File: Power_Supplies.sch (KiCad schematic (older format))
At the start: 82 parts, among them J1 Conn_HDR_2x10_latching, M1 2N7002BK, M2 2N7002BK, Q11 2N7002BK, Q12 2N7002BK, Q13 2N7002BK, Q14 2N7002BK, Q6 2N7002BK, Q7 2N7002BK, Q8 2N7002BK, Q9 2N7002BK, U22 BD50FC0WEFJ-E2, U23 LDL212D33R

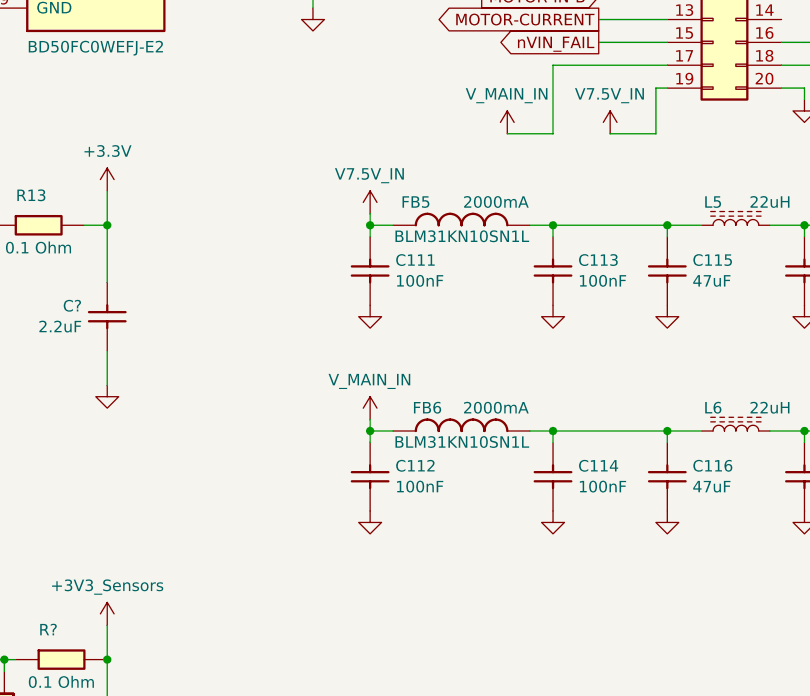
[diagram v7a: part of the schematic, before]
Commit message: Updated BLM31KN102SN1L library part and replaced pre-existing one on Power Supplies sheet
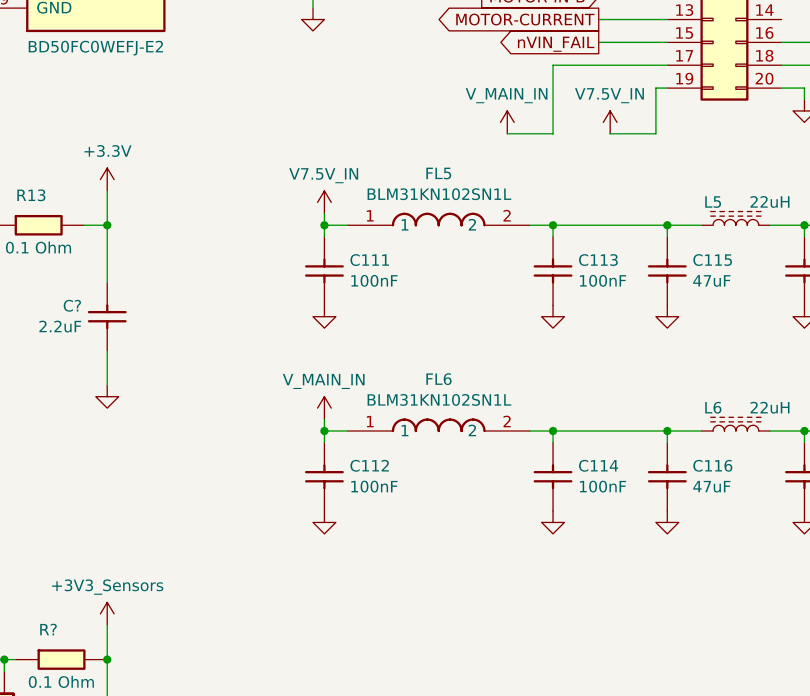
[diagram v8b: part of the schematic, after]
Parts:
- removed FB5, FB6: BLM31KN10SN1L, symbol OpenVent:BLM31KN10SN1L
- added FL5, FL6: BLM31KN102SN1L, BLM31KN102BH1L, symbol OpenVent:BLM31KN102SN1L
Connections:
- net +5V: now also FL5.1
- net V_MAIN: now also FL6.1
- net at C113.1, C115.1, L5.1: now also FL5.2
- net at C114.1, C116.1, L6.1: now also FL6.2
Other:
- moved on the sheet: C111, C112
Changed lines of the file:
@@
 L OpenVent:100nF_0603_Ceramic_Capacitor,_10%,_X7R,_25V C111
 U 1 1 606AB5CB
-P 8350 2550
-F 0 "C111" V 8354 2560 50  0000 L CNN
-F 1 "100nF_0603_Ceramic_Capacitor,_10%,_X7R,_25V" H 8350 2550 50  0001 C CNN
-F 2 "" H 8350 2550 50  0001 C CNN
-F 3 "" H 8350 2550 50  0001 C CNN
-F 4 "100nF" V 8445 2560 50  0000 L CNN "Val"
-F 5 "25V" H 8350 2550 50  0001 C CNN "Voltage"
-F 6 "10%" H 8350 2550 50  0001 C CNN "Tolerance"
-	1    8350 2550
+P 8150 2550
+F 0 "C111" V 8154 2560 50  0000 L CNN
+F 1 "100nF_0603_Ceramic_Capacitor,_10%,_X7R,_25V" H 8150 2550 50  0001 C CNN
+F 2 "" H 8150 2550 50  0001 C CNN
+F 3 "" H 8150 2550 50  0001 C CNN
+F 4 "100nF" V 8245 2560 50  0000 L CNN "Val"
+F 5 "25V" H 8150 2550 50  0001 C CNN "Voltage"
+F 6 "10%" H 8150 2550 50  0001 C CNN "Tolerance"
+	1    8150 2550
 	0    1    1    0
 $EndComp
@@
 	0    -1   -1   0
 $EndComp
-$Comp
-L OpenVent:BLM31KN10SN1L FB5
-U 1 1 60812B24
-P 8600 2400
-F 0 "FB5" H 8450 2500 50  0000 C CNN
-F 1 "BLM31KN10SN1L" H 8650 2350 50  0000 C CNN
-F 2 "" H 8350 2400 50  0001 C CNN
-F 3 "https://drive.google.com/drive/u/1/folders/1bT0MezjjDfDXdTdQktjf6O5y5oTJs8ND" H 8350 2400 50  0001 C CNN
-F 4 "75mR" H 8825 2525 50  0001 L CNN "Val"
-F 5 "2000mA" H 8800 2500 50  0000 C CNN "Current"
-	1    8600 2400
-	1    0    0    -1
-$EndComp
-Wire Wire Line
-	8350 2400 8250 2400
-Wire Wire Line
-	8250 2400 8250 2350
-Wire Wire Line
-	8250 2450 8250 2400
-Connection ~ 8250 2400
+Wire Wire Line
+	8150 2400 8050 2400
+Wire Wire Line
+	8050 2400 8050 2350
+Wire Wire Line
+	8050 2450 8050 2400
+Connection ~ 8050 2400
 Wire Wire Line
 	8950 2400 9050 2400
@@
 L OpenVent:GND #PWR0198
 U 1 1 6087AC95
-P 8250 2750
-F 0 "#PWR0198" H 8250 2500 50  0001 C CNN
-F 1 "GND" H 8250 2600 50  0001 C CNN
-F 2 "" H 8250 2750 50  0001 C CNN
-F 3 "" H 8250 2750 50  0001 C CNN
-	1    8250 2750
+P 8050 2750
+F 0 "#PWR0198" H 8050 2500 50  0001 C CNN
+F 1 "GND" H 8050 2600 50  0001 C CNN
+F 2 "" H 8050 2750 50  0001 C CNN
+F 3 "" H 8050 2750 50  0001 C CNN
+	1    8050 2750
 	1    0    0    -1
 $EndComp
@@
 L OpenVent:V7.5V_IN #PWR0197
 U 1 1 608A108E
-P 8250 2350
-F 0 "#PWR0197" H 8250 2200 50  0001 C CNN
-F 1 "V7.5V_IN" H 8250 2523 50  0000 C CNN
-F 2 "" H 8250 2350 50  0001 C CNN
-F 3 "" H 8250 2350 50  0001 C CNN
-	1    8250 2350
+P 8050 2350
+F 0 "#PWR0197" H 8050 2200 50  0001 C CNN
+F 1 "V7.5V_IN" H 8050 2523 50  0000 C CNN
+F 2 "" H 8050 2350 50  0001 C CNN
+F 3 "" H 8050 2350 50  0001 C CNN
+	1    8050 2350
 	1    0    0    -1
 $EndComp
@@
 L OpenVent:100nF_0603_Ceramic_Capacitor,_10%,_X7R,_25V C112
 U 1 1 6090A7D3
-P 8350 3450
-F 0 "C112" V 8354 3460 50  0000 L CNN
-F 1 "100nF_0603_Ceramic_Capacitor,_10%,_X7R,_25V" H 8350 3450 50  0001 C CNN
-F 2 "" H 8350 3450 50  0001 C CNN
-F 3 "" H 8350 3450 50  0001 C CNN
-F 4 "100nF" V 8445 3460 50  0000 L CNN "Val"
-F 5 "25V" H 8350 3450 50  0001 C CNN "Voltage"
-F 6 "10%" H 8350 3450 50  0001 C CNN "Tolerance"
-	1    8350 3450
+P 8150 3450
+F 0 "C112" V 8154 3460 50  0000 L CNN
+F 1 "100nF_0603_Ceramic_Capacitor,_10%,_X7R,_25V" H 8150 3450 50  0001 C CNN
+F 2 "" H 8150 3450 50  0001 C CNN
+F 3 "" H 8150 3450 50  0001 C CNN
+F 4 "100nF" V 8245 3460 50  0000 L CNN "Val"
+F 5 "25V" H 8150 3450 50  0001 C CNN "Voltage"
+F 6 "10%" H 8150 3450 50  0001 C CNN "Tolerance"
+	1    8150 3450
 	0    1    1    0
 $EndComp
@@
 	0    1    1    0
 $EndComp
-$Comp
-L OpenVent:BLM31KN10SN1L FB6
-U 1 1 6090A817
-P 8600 3300
-F 0 "FB6" H 8500 3400 50  0000 C CNN
-F 1 "BLM31KN10SN1L" H 8650 3250 50  0000 C CNN
-F 2 "" H 8350 3300 50  0001 C CNN
-F 3 "https://drive.google.com/drive/u/1/folders/1bT0MezjjDfDXdTdQktjf6O5y5oTJs8ND" H 8350 3300 50  0001 C CNN
-F 4 "75mR" H 8825 3425 50  0001 L CNN "Val"
-F 5 "2000mA" H 8800 3400 50  0000 C CNN "Current"
-	1    8600 3300
-	1    0    0    -1
-$EndComp
-Wire Wire Line
-	8350 3300 8250 3300
-Wire Wire Line
-	8250 3300 8250 3250
-Wire Wire Line
-	8250 3350 8250 3300
-Connection ~ 8250 3300
+Wire Wire Line
+	8150 3300 8050 3300
+Wire Wire Line
+	8050 3300 8050 3250
+Wire Wire Line
+	8050 3350 8050 3300
+Connection ~ 8050 3300
 Wire Wire Line
 	8950 3300 9050 3300
@@
 L OpenVent:GND #PWR0200
 U 1 1 6090A846
-P 8250 3650
-F 0 "#PWR0200" H 8250 3400 50  0001 C CNN
-F 1 "GND" H 8250 3500 50  0001 C CNN
-F 2 "" H 8250 3650 50  0001 C CNN
-F 3 "" H 8250 3650 50  0001 C CNN
-	1    8250 3650
+P 8050 3650
+F 0 "#PWR0200" H 8050 3400 50  0001 C CNN
+F 1 "GND" H 8050 3500 50  0001 C CNN
+F 2 "" H 8050 3650 50  0001 C CNN
+F 3 "" H 8050 3650 50  0001 C CNN
+	1    8050 3650
 	1    0    0    -1
 $EndComp
@@
 L OpenVent:V_MAIN_IN #PWR0199
 U 1 1 6094290D
-P 8250 3250
-F 0 "#PWR0199" H 8250 3100 50  0001 C CNN
-F 1 "V_MAIN_IN" H 8250 3423 50  0000 C CNN
-F 2 "" H 8250 3250 50  0001 C CNN
-F 3 "" H 8250 3250 50  0001 C CNN
-	1    8250 3250
+P 8050 3250
+F 0 "#PWR0199" H 8050 3100 50  0001 C CNN
+F 1 "V_MAIN_IN" H 8050 3423 50  0000 C CNN
+F 2 "" H 8050 3250 50  0001 C CNN
+F 3 "" H 8050 3250 50  0001 C CNN
+	1    8050 3250
 	1    0    0    -1
 $EndComp
@@
 Wire Wire Line
 	3950 2650 3950 2850
+$Comp
+L OpenVent:BLM31KN102SN1L FL5
+U 1 1 60A84874
+P 8550 2400
+F 0 "FL5" H 8550 2625 50  0000 C CNN
+F 1 "BLM31KN102SN1L" H 8550 2534 50  0000 C CNN
+F 2 "BLM31KN102BH1L" H 9200 2500 50  0001 L CNN
+F 3 "https://www.murata.com/en-us/products/productdetail?partno=BLM31KN102SN1%23" H 9200 2400 50  0001 L CNN
+F 4 "BLM31_N1L Series EMI Suppression Filter 1000+/-25% at 100MHz 2A @85" H 9200 2300 50  0001 L CNN "Description"
+F 5 "1.8" H 9200 2200 50  0001 L CNN "Height"
+F 6 "Murata Electronics" H 9200 2100 50  0001 L CNN "Manufacturer_Name"
+F 7 "BLM31KN102SN1L" H 9200 2000 50  0001 L CNN "Manufacturer_Part_Number"
+F 8 "81-BLM31KN102SN1L" H 9200 1900 50  0001 L CNN "Mouser Part Number"
+F 9 "https://www.mouser.co.uk/ProductDetail/Murata-Electronics/BLM31KN102SN1L?qs=EU6FO9ffTwejecrr1PsOMA%3D%3D" H 9200 1800 50  0001 L CNN "Mouser Price/Stock"
+F 10 "BLM31KN102SN1L" H 9200 1700 50  0001 L CNN "Arrow Part Number"
+F 11 "https://www.arrow.com/en/products/blm31kn102sn1l/murata-manufacturing" H 9200 1600 50  0001 L CNN "Arrow Price/Stock"
+	1    8550 2400
+	1    0    0    -1
+$EndComp
+$Comp
+L OpenVent:BLM31KN102SN1L FL6
+U 1 1 60A86507
+P 8550 3300
+F 0 "FL6" H 8550 3525 50  0000 C CNN
+F 1 "BLM31KN102SN1L" H 8550 3434 50  0000 C CNN
+F 2 "BLM31KN102BH1L" H 9200 3400 50  0001 L CNN
+F 3 "https://www.murata.com/en-us/products/productdetail?partno=BLM31KN102SN1%23" H 9200 3300 50  0001 L CNN
+F 4 "BLM31_N1L Series EMI Suppression Filter 1000+/-25% at 100MHz 2A @85" H 9200 3200 50  0001 L CNN "Description"
+F 5 "1.8" H 9200 3100 50  0001 L CNN "Height"
+F 6 "Murata Electronics" H 9200 3000 50  0001 L CNN "Manufacturer_Name"
+F 7 "BLM31KN102SN1L" H 9200 2900 50  0001 L CNN "Manufacturer_Part_Number"
+F 8 "81-BLM31KN102SN1L" H 9200 2800 50  0001 L CNN "Mouser Part Number"
+F 9 "https://www.mouser.co.uk/ProductDetail/Murata-Electronics/BLM31KN102SN1L?qs=EU6FO9ffTwejecrr1PsOMA%3D%3D" H 9200 2700 50  0001 L CNN "Mouser Price/Stock"
+F 10 "BLM31KN102SN1L" H 9200 2600 50  0001 L CNN "Arrow Part Number"
+F 11 "https://www.arrow.com/en/products/blm31kn102sn1l/murata-manufacturing" H 9200 2500 50  0001 L CNN "Arrow Price/Stock"
+	1    8550 3300
+	1    0    0    -1
+$EndComp
 $EndSCHEMATC
